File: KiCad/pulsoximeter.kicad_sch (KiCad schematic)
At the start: 5 parts, among them Q1 PMOS, SW1 SW_Push, U1 PICO W

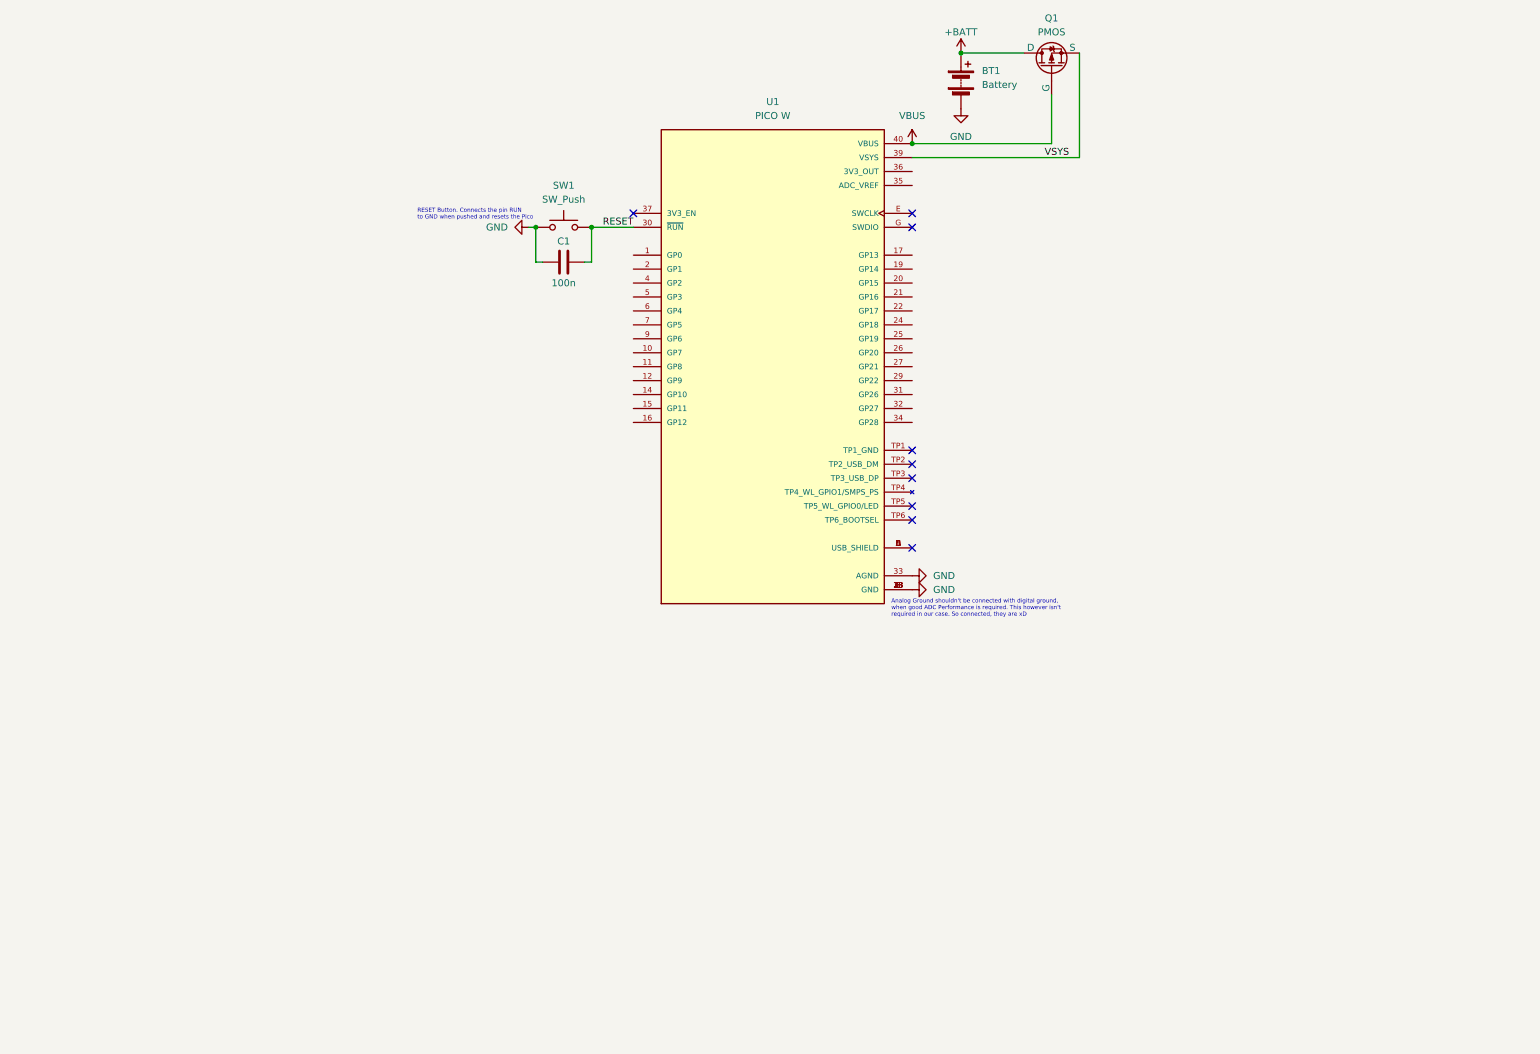
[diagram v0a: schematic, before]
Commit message: Finished schematic and footprint assignment
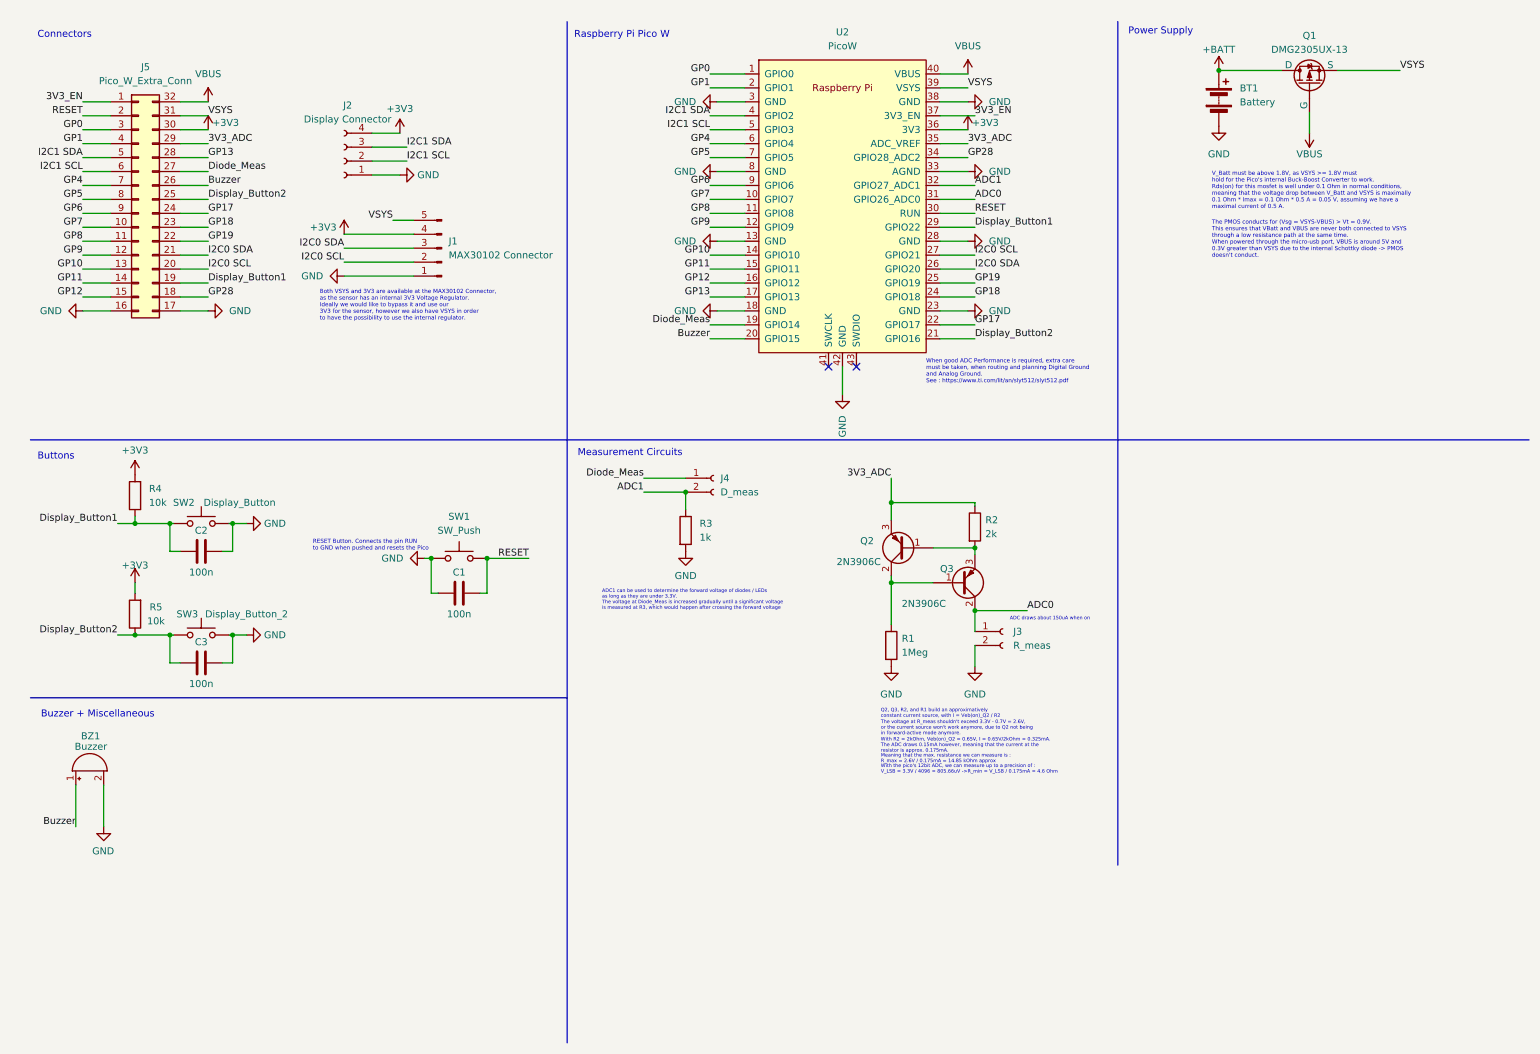
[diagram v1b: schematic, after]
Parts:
- removed U1: PICO W, MODULE_SC0918, symbol PicoW:SC0918
- added BZ1: Buzzer, Buzzer_Beeper:Buzzer_12x9.5RM7.6, symbol Device:Buzzer
- added C2, C3: 100n, Capacitor_THT:C_Radial_D6.3mm_H5.0mm_P2.50mm, symbol Device:C
- added J1: MAX30102 Connector, Connector_PinHeader_2.54mm:PinHeader_1x05_P2.54mm_Vertical, symbol Connector:Conn_01x05_Pin
- added J2: Display Connector, Connector_PinHeader_2.54mm:PinHeader_1x04_P2.54mm_Vertical, symbol Connector:Conn_01x04_Socket
- added J3: R_meas, Connector_PinSocket_2.54mm:PinSocket_1x02_P2.54mm_Vertical, symbol Connector:Conn_01x02_Socket
- added J4: D_meas, Connector_PinSocket_2.54mm:PinSocket_1x02_P2.54mm_Vertical, symbol Connector:Conn_01x02_Socket
- added J5: Pico_W_Extra_Conn, Connector_PinHeader_2.54mm:PinHeader_2x16_P2.54mm_Vertical, symbol Connector_Generic:Conn_02x16_Counter_Clockwise
- added Q2, Q3: 2N3906C, Package_TO_SOT_THT:TO-92_HandSolder, symbol Device:Q_PNP_BCE
- added R1: 1Meg, Resistor_THT:R_Axial_DIN0204_L3.6mm_D1.6mm_P7.62mm_Horizontal, symbol Device:R
- added R2: 2k, Resistor_THT:R_Axial_DIN0204_L3.6mm_D1.6mm_P7.62mm_Horizontal, symbol Device:R
- added R3: 1k, Resistor_THT:R_Axial_DIN0204_L3.6mm_D1.6mm_P7.62mm_Horizontal, symbol Device:R
- added R4, R5: 10k, Resistor_THT:R_Axial_DIN0204_L3.6mm_D1.6mm_P7.62mm_Horizontal, symbol Device:R
- added SW2: Display_Button, Resistor_THT:R_Axial_DIN0204_L3.6mm_D1.6mm_P5.08mm_Horizontal, symbol Switch:SW_Push
- added SW3: Display_Button_2, Resistor_THT:R_Axial_DIN0204_L3.6mm_D1.6mm_P5.08mm_Horizontal, symbol Switch:SW_Push
- added U2: PicoW, RPi_PicoW:RPi_Pico_SMD_TH, symbol RPi_Pico:PicoW
- BT1: footprint (none) -> footprints:PicoW
- C1: footprint (none) -> Capacitor_THT:C_Radial_D6.3mm_H5.0mm_P2.50mm
- Q1: value PMOS -> DMG2305UX-13; footprint (none) -> Package_TO_SOT_SMD:SOT-23_Handsoldering
- SW1: footprint (none) -> Resistor_THT:R_Axial_DIN0204_L3.6mm_D1.6mm_P5.08mm_Horizontal
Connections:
- net GND: now also BZ1.2 (+), C2.2, C3.2, J1.1 (Pin_1), J2.1 (Pin_1), J3.2 (Pin_2), J5.16 (Pin_16), J5.17 (Pin_17), R1.2, R3.2, SW2.2, SW3.2, U2.13 (GND), U2.18 (GND), U2.23 (GND), U2.28 (GND), U2.3 (GND), U2.33 (AGND), U2.38 (GND), U2.42 (GND), U2.8 (GND)
- net RESET: now also J5.2 (Pin_2), U2.30 (RUN)
- net VBUS: now also J5.32 (Pin_32), U2.40 (VBUS)
- net VSYS: now also J1.5 (Pin_5), J5.31 (Pin_31), U2.39 (VSYS)
- new net: Q2.1 (B), Q3.3 (E), R2.2
- new net: Q2.2 (C), Q3.1 (B), R1.1
- new net +3V3: J1.4 (Pin_4), J2.4 (Pin_4), J5.30 (Pin_30), R4.2, R5.2, U2.36 (3V3)
- new net 3V3_ADC: J5.29 (Pin_29), Q2.3 (E), R2.1, U2.35 (ADC_VREF)
- new net 3V3_EN: J5.1 (Pin_1), U2.37 (3V3_EN)
- new net ADC0: J3.1 (Pin_1), Q3.2 (C), U2.31 (GPIO26_ADC0)
- new net ADC1: J4.2 (Pin_2), R3.1, U2.32 (GPIO27_ADC1)
- new net Buzzer: BZ1.1 (-), J5.26 (Pin_26), U2.20 (GPIO15)
- new net Diode_Meas: J4.1 (Pin_1), J5.27 (Pin_27), U2.19 (GPIO14)
- new net Display_Button1: C2.1, J5.19 (Pin_19), R4.1, SW2.1, U2.29 (GPIO22)
- new net Display_Button2: C3.1, J5.25 (Pin_25), R5.1, SW3.1, U2.21 (GPIO16)
- new net GP0: J5.3 (Pin_3), U2.1 (GPIO0)
- new net GP1: J5.4 (Pin_4), U2.2 (GPIO1)
- new net GP10: J5.13 (Pin_13), U2.14 (GPIO10)
- new net GP11: J5.14 (Pin_14), U2.15 (GPIO11)
- new net GP12: J5.15 (Pin_15), U2.16 (GPIO12)
- new net GP13: J5.28 (Pin_28), U2.17 (GPIO13)
- new net GP17: J5.24 (Pin_24), U2.22 (GPIO17)
- new net GP18: J5.23 (Pin_23), U2.24 (GPIO18)
- new net GP19: J5.22 (Pin_22), U2.25 (GPIO19)
- new net GP28: J5.18 (Pin_18), U2.34 (GPIO28_ADC2)
- new net GP4: J5.7 (Pin_7), U2.6 (GPIO4)
- new net GP5: J5.8 (Pin_8), U2.7 (GPIO5)
- new net GP6: J5.9 (Pin_9), U2.9 (GPIO6)
- new net GP7: J5.10 (Pin_10), U2.10 (GPIO7)
- new net GP8: J5.11 (Pin_11), U2.11 (GPIO8)
- new net GP9: J5.12 (Pin_12), U2.12 (GPIO9)
- new net I2C0 SCL: J1.2 (Pin_2), J5.20 (Pin_20), U2.27 (GPIO21)
- new net I2C0 SDA: J1.3 (Pin_3), J5.21 (Pin_21), U2.26 (GPIO20)
- new net I2C1 SCL: J2.2 (Pin_2), J5.6 (Pin_6), U2.5 (GPIO3)
- new net I2C1 SDA: J2.3 (Pin_3), J5.5 (Pin_5), U2.4 (GPIO2)
- no-connect marks 9 -> 2
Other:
- note added: "ADC draws about 150uA when on"
- note added: "ADC1 can be used to determine the forward voltage of diodes / LEDs as long as they are under 3.3V. The voltage at Diode_Meas is increased gradually until a significant voltage is measured at R3, which would happen after crossing the forward voltage"
- note added: "Both VSYS and 3V3 are available at the MAX30102 Connector, as the sensor has an internal 3V3 Voltage Regulator. Ideally we would like to bypass it and use our 3V3 for the sensor, however we also have VSYS in order to have the possibility to use the internal regulator."
- note added: "Buttons"
- note added: "Buzzer + Miscellaneous"
- note added: "Connectors"
- note added: "Meaning that the max. resistance we can measure is : R_max = 2.6V / 0.175mA = 14.85 kOhm approx"
- note added: "Measurement Circuits"
- note added: "Power Supply"
- note added: "Q2, Q3, R2, and R1 build an approximatively constant current source, with I = Veb(on)_Q2 / R2"
- note added: "Raspberry Pi Pico W"
- note added: "The PMOS conducts for (Vsg = VSYS-VBUS) > Vt = 0.9V. This ensures that VBatt and VBUS are never both connected to VSYS through a low resistance path at the same time. When powered through the micro-usb port, VBUS is around 5V and 0.3V greater than VSYS due to the internal Schottky diode -> PMOS doesn't conduct."
- note added: "The voltage at R_meas shouldn't exceed 3.3V - 0.7V = 2.6V, or the current source won't work anymore, due to Q2 not being in forward-active mode anymore."
- note added: "V_Batt must be above 1.8V, as VSYS >= 1.8V must hold for the Pico's internal Buck-Boost Converter to work. Rds(on) for this mosfet is well under 0.1 Ohm in normal conditions, meaning that the voltage drop between V_Batt and VSYS is maximally 0.1 Ohm * Imax = 0.1 Ohm * 0.5 A = 0.05 V, assuming we have a maximal current of 0.5 A."
- note added: "When good ADC Performance is required, extra care must be taken, when routing and planning Digital Ground and Analog Ground. See : https://www.ti.com/lit/an/slyt512/slyt512.pdf"
- note added: "With R2 = 2kOhm, Veb(on)_Q2 = 0.65V, I = 0.65V/2kOhm = 0.325mA. The ADC draws 0.15mA however, meaning that the current at the resistor is approx. 0.175mA."
- note added: "With the pico's 12bit ADC, we can measure up to a precision of : V_LSB = 3.3V / 4096 = 805.66uV ->R_min = V_LSB / 0.175mA = 4.6 Ohm"
- note removed: "Analog Ground shouldn't be connected with digital ground, when good ADC Performance is required. This however isn't required in our case. So connected, they are xD"
- moved on the sheet: BT1, C1, Q1, SW1

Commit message: PCB Design V1 is mostly done. Still have to add some cool art
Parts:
- removed J5: Pico_W_Extra_Conn, Connector_PinHeader_2.54mm:PinHeader_2x16_P2.54mm_Vertical, symbol Connector_Generic:Conn_02x16_Counter_Clockwise
- added J5: Analog, Connector_PinHeader_2.54mm:PinHeader_1x20_P2.54mm_Vertical, symbol Connector:Conn_01x20_Pin
- added J7: Digital, Connector_PinHeader_2.54mm:PinHeader_1x20_P2.54mm_Vertical, symbol Connector:Conn_01x20_Pin
- BT1: footprint footprints:PicoW -> Battery:BatteryHolder_Keystone_2479_3xAAA
- J1: value MAX30102 Connector -> MAX30102
- U2: footprint RPi_PicoW:RPi_Pico_SMD_TH -> RPi_Pico:RPi_PicoW_SMD_TH
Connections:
- net GP13 is gone; now on net Display_Button2: U2.17 (GPIO13)
- net GP4 is gone; now on net I2C0 SDA: U2.6 (GPIO4)
- net GP5 is gone; now on net I2C0 SCL: U2.7 (GPIO5)
- net GP9 is gone; now on net Display_Button1: U2.12 (GPIO9)
- net +3V3: now also J5.5 (Pin_5)
- net 3V3_ADC: now also J5.6 (Pin_6)
- net 3V3_EN: now also J5.4 (Pin_4)
- net ADC0: now also J4.2 (Pin_2), R3.1, J5.10 (Pin_10); no longer J3.1 (Pin_1), Q3.2 (C)
- net ADC1: now also J3.1 (Pin_1), Q3.2 (C), J5.9 (Pin_9); no longer J4.2 (Pin_2), R3.1
- net Buzzer: now also J7.1 (Pin_1)
- net Diode_Meas: now also U2.29 (GPIO22), J5.12 (Pin_12); no longer U2.19 (GPIO14)
- net Display_Button1: now also J7.9 (Pin_9); no longer U2.29 (GPIO22)
- net Display_Button2: now also J7.4 (Pin_4); no longer U2.21 (GPIO16)
- net GND: now also J5.13 (Pin_13), J5.18 (Pin_18), J5.3 (Pin_3), J5.8 (Pin_8), J7.13 (Pin_13), J7.18 (Pin_18), J7.3 (Pin_3), J7.8 (Pin_8); no longer U2.42 (GND)
- net GP0: now also J7.20 (Pin_20)
- net GP1: now also J7.19 (Pin_19)
- net GP10: now also J7.7 (Pin_7)
- net GP11: now also J7.6 (Pin_6)
- net GP12: now also J7.5 (Pin_5)
- net GP17: now also J5.19 (Pin_19)
- net GP18: now also J5.17 (Pin_17)
- net GP19: now also J5.16 (Pin_16)
- net GP28: now also J5.7 (Pin_7)
- net GP6: now also J7.12 (Pin_12)
- net GP7: now also J7.11 (Pin_11)
- net GP8: now also J7.10 (Pin_10)
- net I2C0 SCL: now also J2.2 (Pin_2), J7.14 (Pin_14); no longer J1.2 (Pin_2), U2.27 (GPIO21)
- net I2C0 SDA: now also J2.3 (Pin_3), J7.15 (Pin_15); no longer J1.3 (Pin_3), U2.26 (GPIO20)
- net I2C1 SCL: now also J1.2 (Pin_2), J7.16 (Pin_16); no longer J2.2 (Pin_2)
- net I2C1 SDA: now also J1.3 (Pin_3), J7.17 (Pin_17); no longer J2.3 (Pin_3)
- net RESET: now also J5.11 (Pin_11)
- net VSYS: now also J5.1 (Pin_1), J5.2 (Pin_2)
- new net GP14: J7.2 (Pin_2), U2.19 (GPIO14)
- new net GP16: J5.20 (Pin_20), U2.21 (GPIO16)
- new net GP20: J5.15 (Pin_15), U2.26 (GPIO20)
- new net GP21: J5.14 (Pin_14), U2.27 (GPIO21)
- no-connect marks 2 -> 3
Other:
- note added: "ADC0 can be used to determine the forward voltage of diodes / LEDs as long as they are under 3.3V. The voltage at Diode_Meas is increased gradually until a significant voltage is measured at R3, which would happen after crossing the forward voltage"
- note removed: "ADC1 can be used to determine the forward voltage of diodes / LEDs as long as they are under 3.3V. The voltage at Diode_Meas is increased gradually until a significant voltage is measured at R3, which would happen after crossing the forward voltage"
- moved on the sheet: J1, J2
